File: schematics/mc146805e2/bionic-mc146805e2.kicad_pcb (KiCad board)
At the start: 2 copper layers, 27.9 x 68.6 mm, 8 parts, among them J1 Bionic-P135, J2 Bionic-P245, U1 MC146805E2P, U2 11AA010-I/TT

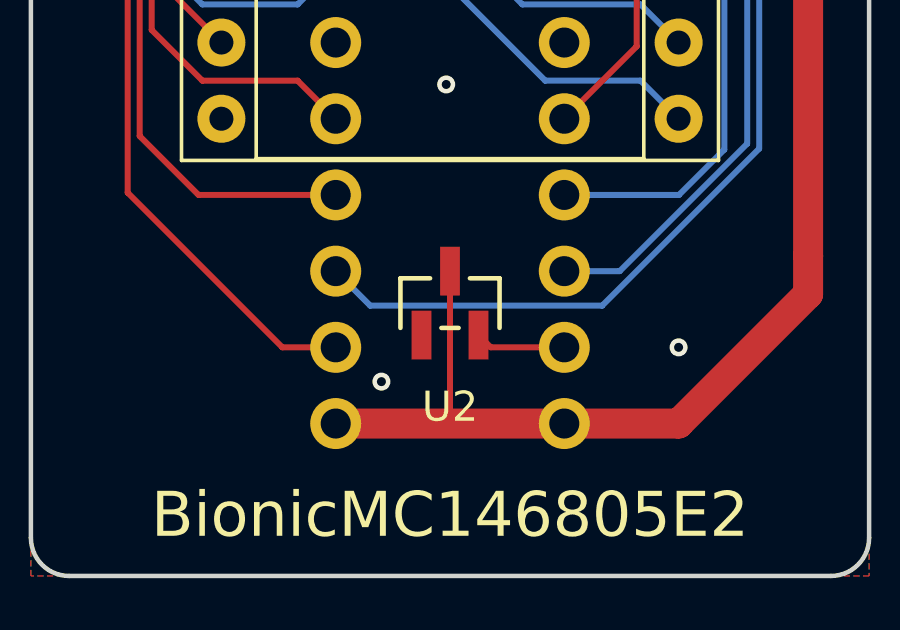
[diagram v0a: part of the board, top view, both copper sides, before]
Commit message: [MC146805E2] Fix EEPROM pinout
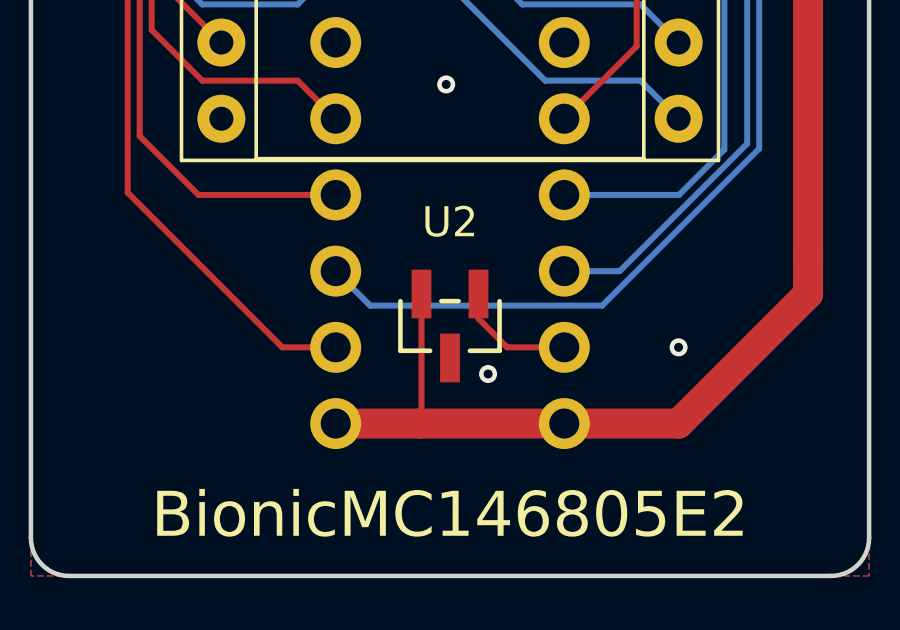
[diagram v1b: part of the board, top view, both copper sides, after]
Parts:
- moved U2 0.76 mm to (115.0, 130.2), turned to 180 degrees
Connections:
- U2 pad 1: GND -> Net-(J2-P57)
- U2 pad 2: Net-(J2-P57) -> VCC
- U2 pad 3: VCC -> GND
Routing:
- net Net-(J2-P57): track 3.03 -> 4.08 mm
- net VCC: track 89.7 -> 89.0 mm
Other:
- board text added: "Rev. 7"
- board text removed: "Rev. 6"
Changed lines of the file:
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@@
   (title_block
     (title "BionicMC146805E2")
-    (date "2024-10-22")
-    (rev "6")
+    (date "2024-11-01")
+    (rev "7")
     (company "Tadashi G. Takaoka")
   )
@@
   (net 48 "unconnected-(U1-OSC2-Pad38)")
   (footprint "0-LocalLibrary:SOT-23_MC_MCH-M" locked (layer "F.Cu")
-    (at 114.97 129.486)
+    (at 114.97 130.248 180)
     (descr "Microchip 11AAxxx-I/TT UNI/O 1Kbit Serial EEPROM")
     (property "Sheetfile" "bionic-mc146805e2.kicad_sch")
@@
         (effects (font (size 1 1) (thickness 0.15)))
     )
-    (fp_text value "11AA010-I/TT" (at 0 0 unlocked) (layer "F.Fab")
+    (fp_text value "11AA010-I/TT" (at 0 0 180 unlocked) (layer "F.Fab")
         (effects (font (size 1 1) (thickness 0.15)))
     )
-    (fp_text user "${REFERENCE}" (at 0 0 unlocked) (layer "F.Fab")
+    (fp_text user "${REFERENCE}" (at 0 0 180 unlocked) (layer "F.Fab")
         (effects (font (size 1 1) (thickness 0.15)))
     )
@@
     (fp_circle (center -1.270999 0.446) (end -1.143999 0.446)
       (stroke (width 0.0254) (type solid)) (fill none) (layer "F.Fab"))
-    (pad "1" smd rect locked (at -0.950001 1.066) (size 0.6604 1.6256) (layers "F.Cu" "F.Paste" "F.Mask")
+    (pad "1" smd rect locked (at -0.950001 1.066 180) (size 0.6604 1.6256) (layers "F.Cu" "F.Paste" "F.Mask")
+      (net 26 "Net-(J2-P57)") (pinfunction "SCIO") (pintype "bidirectional"))
+    (pad "2" smd rect locked (at 0.950001 1.066 180) (size 0.6604 1.6256) (layers "F.Cu" "F.Paste" "F.Mask")
+      (net 1 "VCC") (pinfunction "VCC") (pintype "power_in"))
+    (pad "3" smd rect locked (at 0 -1.066 180) (size 0.6604 1.6256) (layers "F.Cu" "F.Paste" "F.Mask")
       (net 2 "GND") (pinfunction "VSS") (pintype "power_in"))
-    (pad "2" smd rect locked (at 0.950001 1.066) (size 0.6604 1.6256) (layers "F.Cu" "F.Paste" "F.Mask")
-      (net 26 "Net-(J2-P57)") (pinfunction "SCIO") (pintype "bidirectional"))
-    (pad "3" smd rect locked (at 0 -1.066) (size 0.6604 1.6256) (layers "F.Cu" "F.Paste" "F.Mask")
-      (net 1 "VCC") (pinfunction "VCC") (pintype "power_in"))
     (model "${KIPRJMOD}/0-LocalLibrary/SOT-23_MC_MCH.step"
       (offset (xyz 0 0 0))
@@
     (effects (font (size 0.8 0.8)) (justify bottom mirror))
   )
-  (gr_text "Rev. 6\n" (at 107.096 137.31) (layer "B.SilkS")
+  (gr_text "Rev. 7" (at 107.096 137.31) (layer "B.SilkS")
     (effects (font (size 1 1)) (justify left bottom mirror))
   )
@@
   )
   (segment locked (start 126.908 75.588) (end 126.908 75.027) (width 0.2) (layer "F.Cu") (net 1))
-  (segment locked (start 111.16 133.5) (end 118.78 133.5) (width 1) (layer "F.Cu") (net 1))
   (segment (start 119.034 71.524) (end 122.59 75.08) (width 0.2) (layer "F.Cu") (net 1))
   (segment (start 115.7447 71.524) (end 119.034 71.524) (width 0.2) (layer "F.Cu") (net 1))
-  (segment locked (start 114.97 133.5) (end 114.97 128.42) (width 0.2) (layer "F.Cu") (net 1))
   (segment locked (start 126.908 75.588) (end 126.4 75.08) (width 1) (layer "F.Cu") (net 1))
   (segment locked (start 126.908 127.912) (end 126.908 75.842) (width 1) (layer "F.Cu") (net 1))
   (segment locked (start 115.745 71.524) (end 115.7447 71.524) (width 0.2) (layer "F.Cu") (net 1))
+  (segment (start 114.019999 133.434001) (end 113.954 133.5) (width 0.2) (layer "F.Cu") (net 1))
+  (segment (start 113.954 133.5) (end 118.78 133.5) (width 1) (layer "F.Cu") (net 1))
   (segment (start 126.908 75.842) (end 126.908 75.588) (width 1) (layer "F.Cu") (net 1))
+  (segment (start 111.16 133.5) (end 113.954 133.5) (width 1) (layer "F.Cu") (net 1))
   (segment locked (start 125.077 75.08) (end 125.13 75.027) (width 0.2) (layer "F.Cu") (net 1))
   (segment (start 122.59 133.5) (end 126.908 129.182) (width 1) (layer "F.Cu") (net 1))
@@
   (segment (start 126.908 129.182) (end 126.908 127.912) (width 1) (layer "F.Cu") (net 1))
   (segment locked (start 126.4 75.08) (end 122.59 75.08) (width 1) (layer "F.Cu") (net 1))
+  (segment (start 114.019999 129.182) (end 114.019999 133.434001) (width 0.2) (layer "F.Cu") (net 1))
   (via (at 122.59 130.96) (size 0.6) (drill 0.3) (layers "F.Cu" "B.Cu") (free) (net 2))
   (via (at 114.843 122.197) (size 0.6) (drill 0.3) (layers "F.Cu" "B.Cu") (free) (net 2))
   (via (at 114.97 79.017) (size 0.6) (drill 0.3) (layers "F.Cu" "B.Cu") (free) (net 2))
-  (via (at 112.684 132.103) (size 0.6) (drill 0.3) (layers "F.Cu" "B.Cu") (free) (net 2))
+  (via (at 116.24 131.849) (size 0.6) (drill 0.3) (layers "F.Cu" "B.Cu") (free) (net 2))
   (segment (start 114.1953 71.524) (end 112.0725 71.524) (width 0.2) (layer "F.Cu") (net 3))
   (segment (start 117.402 103.42) (end 118.272 104.29) (width 0.2) (layer "B.Cu") (net 4))
@@
   (segment (start 104.226 78.204) (end 107.35 75.08) (width 0.2) (layer "F.Cu") (net 25))
   (segment (start 111.16 130.96) (end 109.382 130.96) (width 0.2) (layer "F.Cu") (net 25))
-  (segment (start 118.78 130.96) (end 116.328001 130.96) (width 0.2) (layer "F.Cu") (net 26))
-  (segment (start 116.328001 130.96) (end 115.920001 130.552) (width 0.2) (layer "F.Cu") (net 26))
+  (segment (start 116.875 130.96) (end 118.78 130.96) (width 0.2) (layer "F.Cu") (net 26))
+  (segment (start 115.920001 129.182) (end 115.920001 130.005001) (width 0.2) (layer "F.Cu") (net 26))
+  (segment (start 115.920001 130.005001) (end 116.875 130.96) (width 0.2) (layer "F.Cu") (net 26))
   (segment (start 124.876 124.171314) (end 124.876 100.226) (width 0.2) (layer "B.Cu") (net 27))
   (segment (start 120.627314 128.42) (end 124.876 124.171314) (width 0.2) (layer "B.Cu") (net 27))

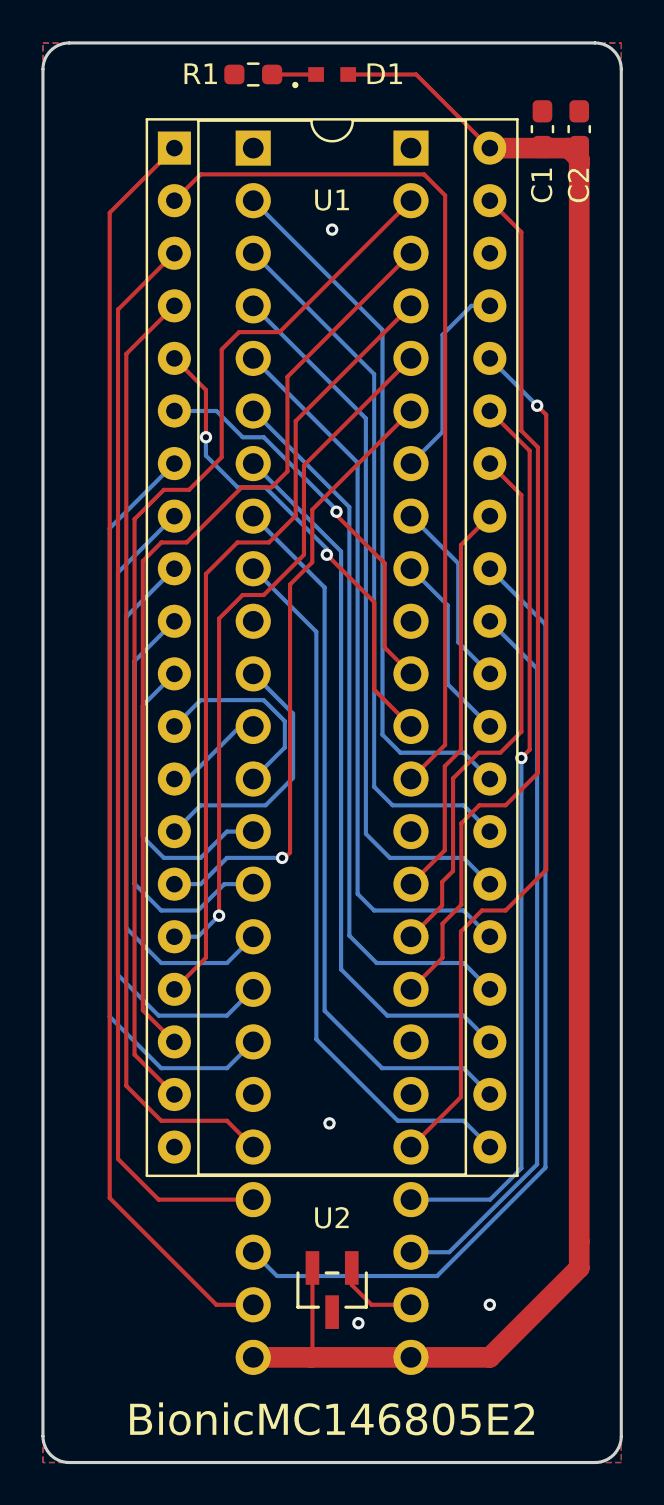
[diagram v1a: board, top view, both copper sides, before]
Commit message: [MC146805E2] Shrink board size
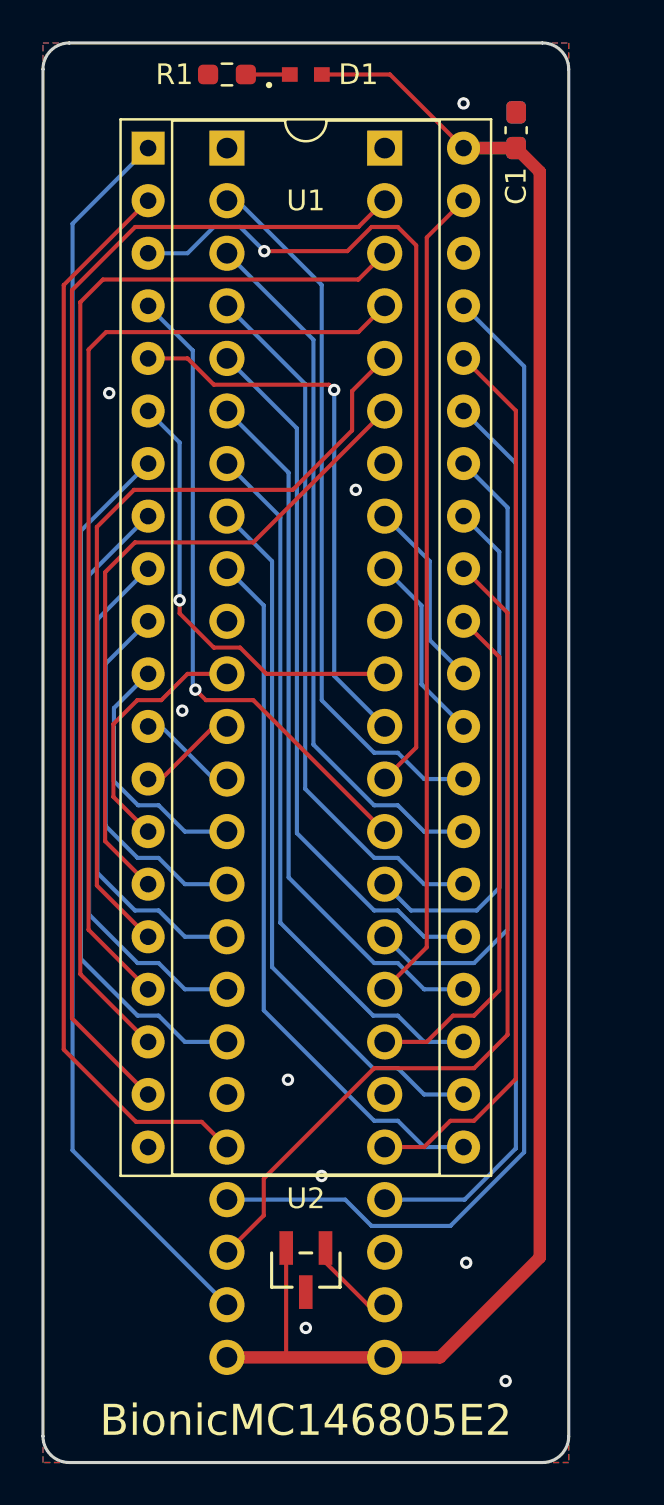
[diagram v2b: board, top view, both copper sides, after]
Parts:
- C2: moved to B.Cu
- moved C2 3.05 mm to (123.9, 74.2)
- moved U2 1.60 mm to (113.7, 129.3)
- moved C1 1.27 mm to (123.9, 74.2)
- moved D1 1.27 mm to (113.7, 71.5)
- moved J1 1.27 mm to (109.9, 75.1)
- moved J2 1.27 mm to (117.5, 75.1)
- moved R1 1.27 mm to (109.9, 71.5)
- moved U1 1.27 mm to (106.1, 75.1)
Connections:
- J2 pad 27: /P56 -> unconnected-(J2-P56-Pad27)
- J2 pad 31: unconnected-(J2-P47-Pad31) -> /P47
- J2 pad 35: unconnected-(J2-P43-Pad35) -> /P43
- J2 pad 42: /P25 -> unconnected-(J2-P25-Pad42)
- U1 pad 2: /P42 -> /P50
- U1 pad 3: /P51 -> /P42
- U1 pad 31: /P56 -> /P47
- U1 pad 37: /P25 -> /P51
- U1 pad 4: /P50 -> /P43
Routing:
- net /P56: track 35.0 -> 0.00 mm
- net /P43: track 0.00 -> 31.5 mm, vias 0 -> 1
- net /P47: track 0.00 -> 25.1 mm
- net /P25: track 9.72 -> 0.00 mm
- net /P22: track 38.6 -> 47.3 mm
- net /P21: track 45.7 -> 52.8 mm
- net /P50: track 46.0 -> 52.5 mm
- net /P51: track 52.2 -> 58.5 mm
- net /P20: track 51.4 -> 57.3 mm
- net /P44: track 19.4 -> 25.2 mm
- net /P23: track 33.9 -> 39.2 mm, vias 1 -> 0
- net /P32: track 9.71 -> 4.86 mm
- net /P52: track 46.8 -> 42.3 mm
- net /P45: track 26.3 -> 30.5 mm
- net /P41: track 23.3 -> 26.9 mm, vias 2 -> 1
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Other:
- board size 27.9 x 68.6 mm -> 25.4 x 68.6 mm
- board text added: "Rev. 8"
- board text removed: "Rev. 7"

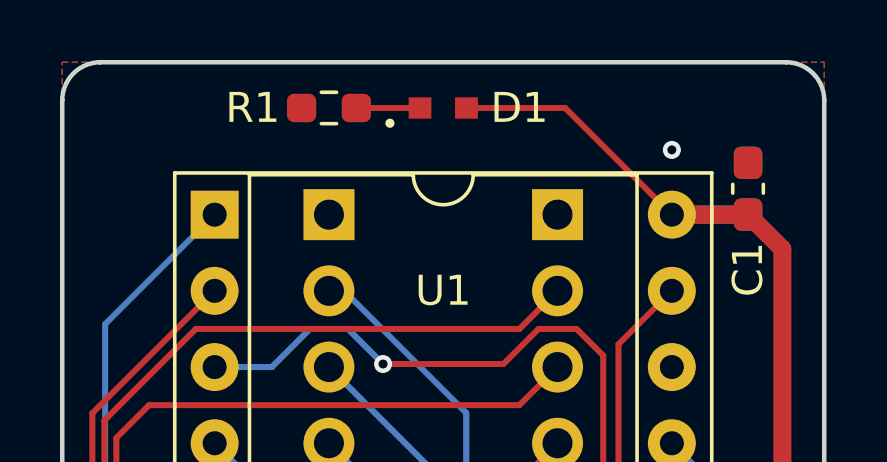
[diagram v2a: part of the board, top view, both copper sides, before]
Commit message: [schematics] Update LED footprint
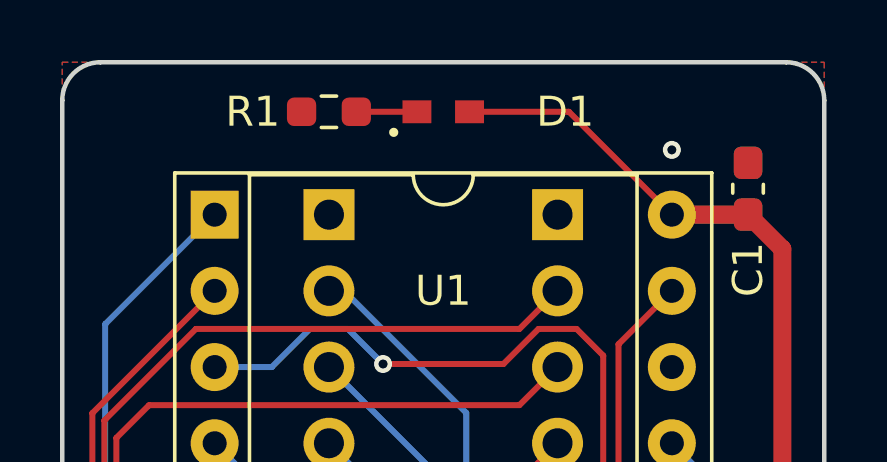
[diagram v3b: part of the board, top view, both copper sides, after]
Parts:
- D1: footprint 0-LocalLibrary:LED_CSL1901UW1_ROM -> 0-LocalLibrary:LED_CSL1901UW1_ROM-M
- J1: footprint connector:Bionic-P135_Vertical -> 0-LocalLibrary:Bionic-P135_Vertical
- J2: footprint connector:Bionic-P245_Vertical -> 0-LocalLibrary:Bionic-P245_Vertical
- moved D1 0.13 mm to (113.7, 71.7)
- moved R1 0.13 mm to (109.9, 71.7)
